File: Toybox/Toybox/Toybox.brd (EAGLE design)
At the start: 98.4 x 30 mm, 28 parts, among them J2 RASPBERRYPI-40-PIN-GPIO, U2 US1881, X1 USB-A-TH

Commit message: Circuit is complete. Add logo if there is time
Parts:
- removed U2: US1881, Toybox:TO-92-3L
- added J5: (no value), SparkFun-Connectors:1X03
- moved R1 8.06 mm to (6.99, 10.2), turned to 180 degrees
- moved R8 1.89 mm to (6.99, 6.86)
- moved R4 1.40 mm to (32.4, 1.65)
- moved T1 1.18 mm to (13.5, 6.84)
- moved C7 0.74 mm to (46.6, 5.97)
- moved J1 0.64 mm to (91.8, 26.7)
- moved R6 0.63 mm to (13.5, 10.2)
- moved R9 0.31 mm to (49.1, 5.97), turned to 270 degrees
- moved JP2 0.28 mm to (19.8, 1.91)
- moved J3 0.26 mm to (6.99, 1.91)
- moved R5 0.25 mm to (26.0, 5.59)
- moved JP1 0.25 mm to (26.0, 1.91)
- moved R7 0.20 mm to (19.8, 5.59)
- moved C6 0.16 mm to (51.7, 5.97)
- moved J4 0.15 mm to (37.1, 1.91)
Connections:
- removed net 3.3V: J2.1, J2.17
- new net NC1: J2.1
- new net NC2: J2.17
- net 5V: now also J5.1, R9.2; no longer R9.1, U2.1
- net GND: now also J5.3; no longer U2.3
- net HALL_SENSOR: now also J5.2, R9.1; no longer R9.2, U2.2
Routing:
- net 5V: track 19.0 -> 143.9 mm, vias 0 -> 3
- net HALL_SENSOR: track 0.00 -> 44.2 mm
- net ON_BUTTON: track 0.00 -> 29.8 mm
- net SERVO_PWM: track 0.00 -> 27.3 mm, vias 0 -> 2
- net N$2: track 0.00 -> 22.1 mm
- net PWR_LED: track 0.00 -> 16.4 mm
- net N$8: track 0.00 -> 12.2 mm
- net N$9: track 0.00 -> 10.3 mm
- net N$7: track 0.00 -> 10.1 mm
- net N$1: track 0.00 -> 6.01 mm
- net N$4: track 0.00 -> 2.47 mm
- added copper zone on layer 1, net GND
- added copper zone on layer 16, net GND
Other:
- board text added: "5V"
- board text added: "BUTTON"
- board text added: "GND"
- board text added: "HALL SENSOR"
- board text added: "LED +"
- board text added: "LED -"
- board text added: "POWER BUTTON"
- board text added: "SERVO"
- board text added: "SIGNAL"

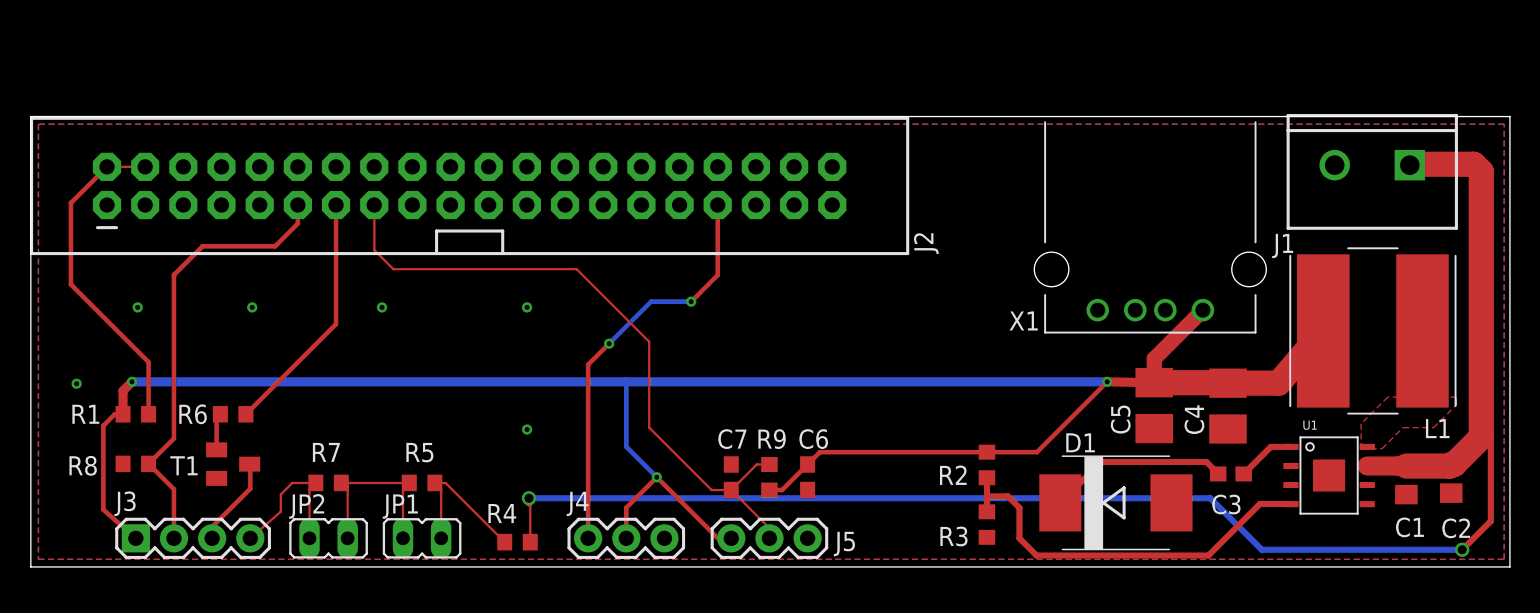
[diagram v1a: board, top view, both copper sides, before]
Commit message: Removing the ignored files. Started personal DRU and CAM folder. Created BOM
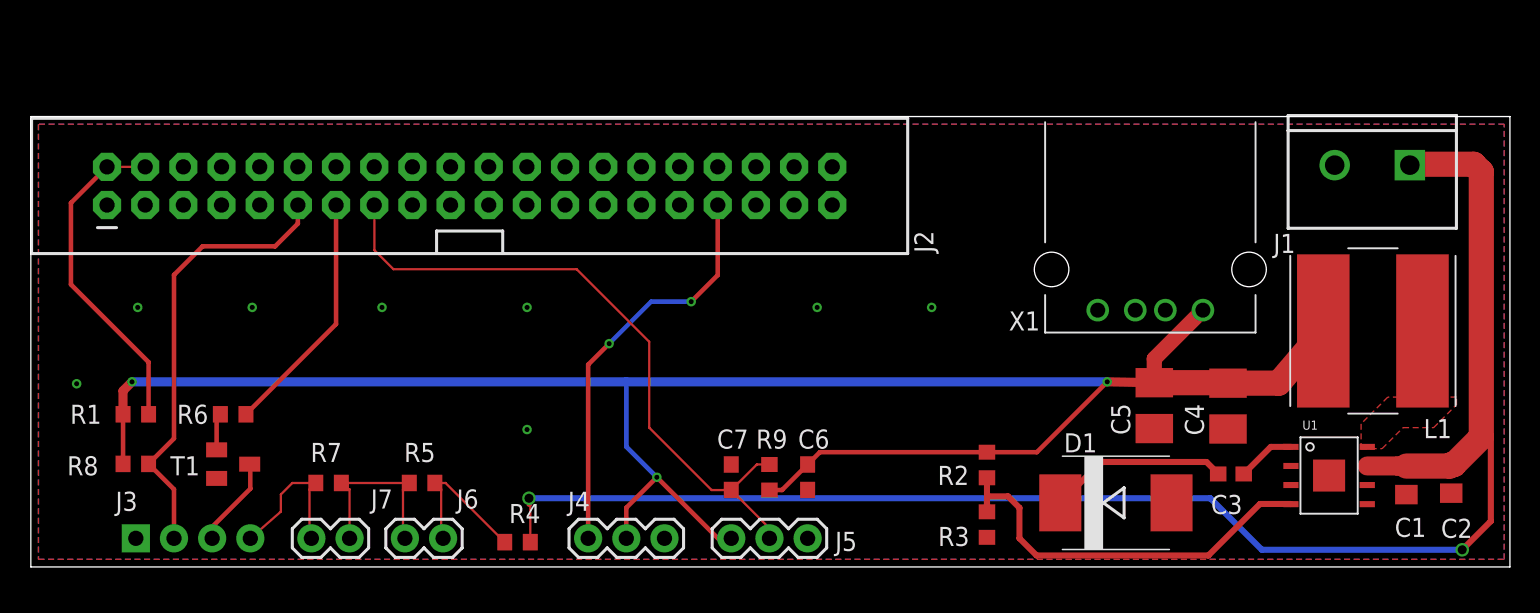
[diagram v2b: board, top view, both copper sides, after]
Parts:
- removed JP1, JP2: (no value), jumper:JP1
- added J6, J7: (no value), SparkFun-Connectors:1X02
- J3: device SparkFun-Connectors:1X04 -> SparkFun-Connectors:1X04_NO_SILK
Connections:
- net 5V: now also R8.1; no longer J3.1
- net GND: now also J3.1; no longer R8.1
- net N$7: now also J6.1; no longer JP1.2
- net N$8: now also J6.2, J7.1; no longer JP1.1, JP2.2
- net N$9: now also J7.2; no longer JP2.1
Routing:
- net 5V: track 143.9 -> 137.1 mm

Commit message: Fixed up the toybox board. Added different passive components all around
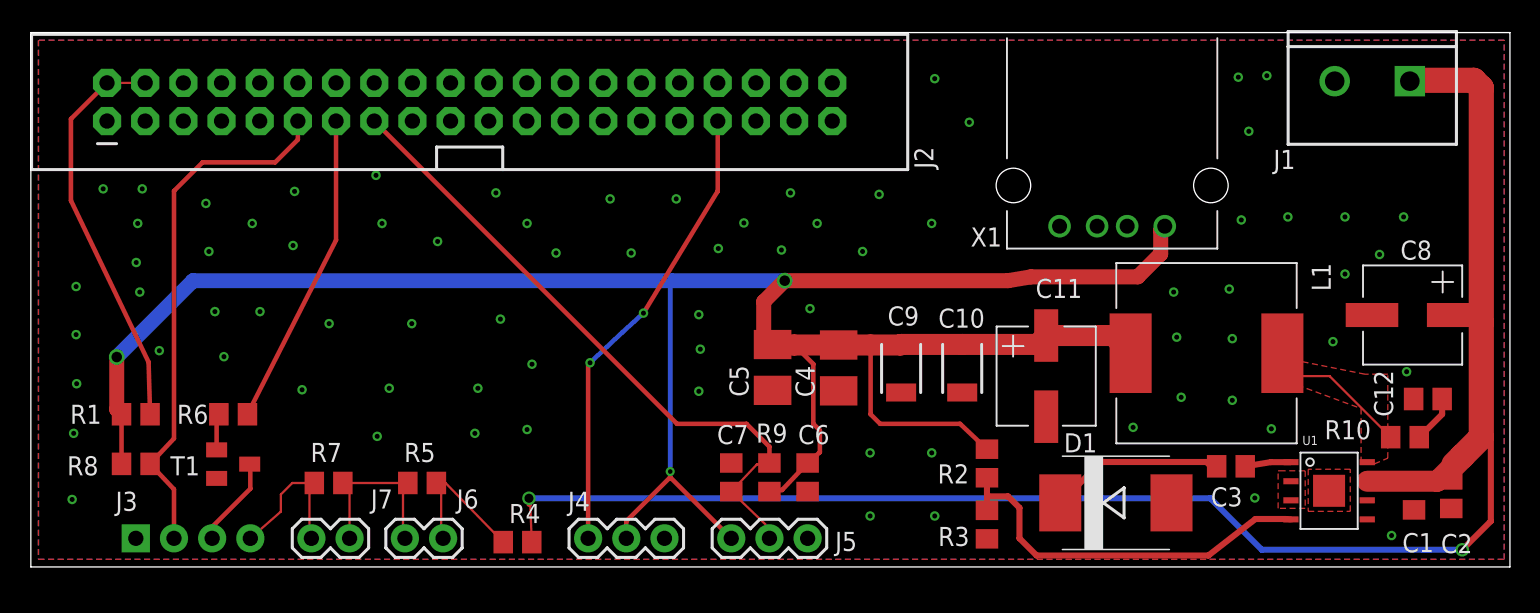
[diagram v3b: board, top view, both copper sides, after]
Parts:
- added C10, C9: 47uF, SparkFun-Passives:1210
- added C11, C8: 47uF, Master:CPOL-RADIAL-6.3
- added C12: (no value), resistor:C0805
- added R10: (no value), resistor:R0805
- C3, C6, C7: device resistor:C0603 -> resistor:C0805
- L1: value 10uH -> 22uH; device Toybox:SRN1060 -> Master:IND-SRR1210
- R1, R2, R3, R4, R5, R6, R7, R8, R9: device resistor:R0603 -> resistor:R0805
- moved C4 26.0 mm to (53.8, 13.2)
- moved C5 25.5 mm to (49.4, 13.3)
- moved L1 11.2 mm to (78.2, 14.2), turned to 270 degrees
- moved X1 6.14 mm to (72.0, 28.7)
- moved J1 5.59 mm to (91.8, 32.3)
- moved J2 5.59 mm to (29.2, 30.9)
- moved C1 1.14 mm to (92.0, 4.75)
- moved C2 1.02 mm to (94.5, 4.84)
- moved U1 1.02 mm to (86.4, 5.07)
- moved C3 0.51 mm to (79.9, 6.70)
- moved R2 0.10 mm to (63.6, 6.89)
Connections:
- new net N$10: C12.2, R10.1
- net 5V: now also C10.1, C11.1, C9.1, L1.P$2; no longer L1.2
- net GND: now also C10.2, C11.2, C12.1, C8.2, C9.2, U1.2, U1.3
- net SW: now also L1.P$1, R10.2; no longer L1.1
- net VCC: now also C8.1
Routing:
- net 5V: track 137.1 -> 162.6 mm
- net SW: track 0.00 -> 10.4 mm
- net VCC: track 105.9 -> 115.1 mm
- net ON_BUTTON: track 29.8 -> 35.3 mm
- net N$2: track 22.1 -> 26.8 mm
- net PWR_LED: track 16.4 -> 20.9 mm
- net SERVO_PWM: track 27.3 -> 30.8 mm
- net N$10: track 0.00 -> 3.17 mm
- net N$6: track 3.89 -> 3.06 mm
- net N$3: track 27.8 -> 27.0 mm
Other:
- board size 98.4 x 30 mm -> 98.4 x 35.6 mm
- board text added: "+"
- board text added: "-"
